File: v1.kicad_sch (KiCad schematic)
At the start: 8 parts, among them J1 Screw_Terminal_01x04, U2 ESP32 DevKitV1 DoIt, U4 AHT20 Humidity Module

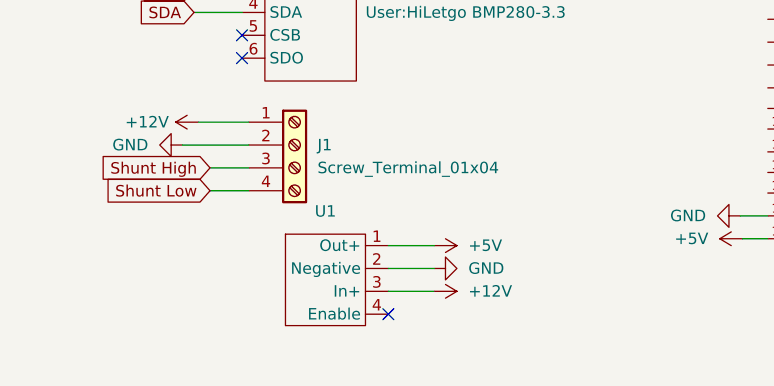
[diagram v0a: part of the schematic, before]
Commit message: Working on alternave voltage converter
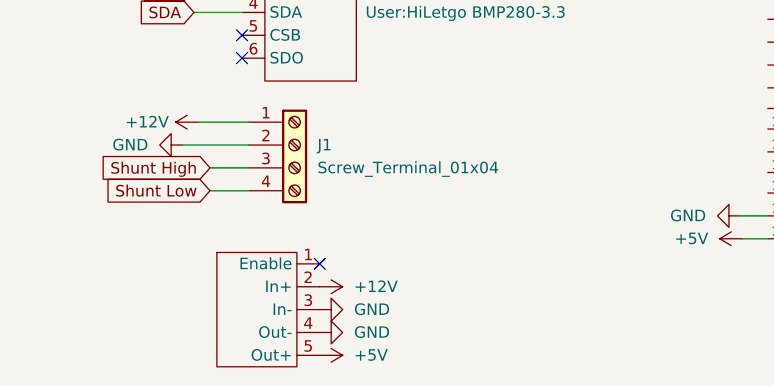
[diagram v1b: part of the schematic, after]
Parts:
- removed U1: ~, User:Drok Vreg, symbol User:Drok_Vreg
- added U5: ~, User:Drok Vreg_5pin, symbol User:Drok_Vreg_5Pin
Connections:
- net +12V: now also U5.2 (In+)
- net +5V: now also U5.5 (Out+)
- net GND: now also U5.3 (In-), U5.4 (Out-)

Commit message: Version 1.2 pcb, 3.3 volt adc, updated step down
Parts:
- R1: value 10000 -> 36000
- R2: value 5000 -> 10000
- renumbered U5 to U1
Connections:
- net +3V3: now also M1.1 (VDD), U1.5 (Out+)
- removed net +5V: M1.1 (VDD), U1.5 (Out+), U2.15 (VIN)
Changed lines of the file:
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@@
 	(wire
 		(pts
-			(xy 96.52 100.076) (xy 99.314 100.076)
+			(xy 37.338 92.202) (xy 41.656 92.202)
 		)
 		(stroke
@@
 	(wire
 		(pts
-			(xy 37.338 92.202) (xy 41.656 92.202)
+			(xy 96.266 97.536) (xy 99.314 97.536)
 		)
 		(stroke
@@
 	(wire
 		(pts
-			(xy 96.266 97.536) (xy 99.314 97.536)
+			(xy 36.068 87.122) (xy 41.656 87.122)
 		)
 		(stroke
@@
 	(wire
 		(pts
-			(xy 36.068 87.122) (xy 41.656 87.122)
+			(xy 25.4 36.068) (xy 29.464 36.068)
 		)
 		(stroke
@@
 	(wire
 		(pts
-			(xy 25.4 36.068) (xy 29.464 36.068)
+			(xy 34.29 89.662) (xy 41.656 89.662)
 		)
 		(stroke
@@
 	(wire
 		(pts
-			(xy 34.29 89.662) (xy 41.656 89.662)
+			(xy 111.76 50.292) (xy 116.332 50.292)
 		)
 		(stroke
@@
 	(wire
 		(pts
-			(xy 111.76 50.292) (xy 116.332 50.292)
+			(xy 43.434 26.416) (xy 43.434 30.988)
 		)
 		(stroke
@@
 	(wire
 		(pts
-			(xy 43.434 26.416) (xy 43.434 30.988)
+			(xy 43.434 52.578) (xy 43.434 56.134)
 		)
 		(stroke
@@
 	(wire
 		(pts
-			(xy 43.434 52.578) (xy 43.434 56.134)
+			(xy 110.49 26.416) (xy 114.3 26.416)
 		)
 		(stroke
@@
 	(wire
 		(pts
-			(xy 110.49 26.416) (xy 114.3 26.416)
+			(xy 124.206 97.79) (xy 130.81 97.79)
 		)
 		(stroke
@@
 	(wire
 		(pts
-			(xy 124.206 97.79) (xy 130.81 97.79)
+			(xy 83.566 26.416) (xy 86.36 26.416)
 		)
 		(stroke
@@
 	(wire
 		(pts
-			(xy 83.566 26.416) (xy 86.36 26.416)
+			(xy 56.134 47.498) (xy 60.96 47.498)
 		)
 		(stroke
@@
 	(wire
 		(pts
-			(xy 56.134 47.498) (xy 60.96 47.498)
+			(xy 99.568 36.068) (xy 99.568 26.416)
 		)
 		(stroke
@@
 	(wire
 		(pts
-			(xy 99.568 36.068) (xy 99.568 26.416)
+			(xy 35.56 67.31) (xy 40.894 67.31)
 		)
 		(stroke
@@
 	(wire
 		(pts
-			(xy 35.56 67.31) (xy 40.894 67.31)
+			(xy 37.338 94.742) (xy 41.656 94.742)
 		)
 		(stroke
@@
 	(wire
 		(pts
-			(xy 37.338 94.742) (xy 41.656 94.742)
+			(xy 56.134 36.068) (xy 99.568 36.068)
 		)
 		(stroke
@@
 	(wire
 		(pts
-			(xy 56.134 36.068) (xy 99.568 36.068)
+			(xy 24.638 43.688) (xy 29.464 43.688)
 		)
 		(stroke
@@
 	(wire
 		(pts
-			(xy 24.638 43.688) (xy 29.464 43.688)
+			(xy 35.56 74.93) (xy 40.894 74.93)
 		)
 		(stroke
@@
 		)
 	)
-	(wire
-		(pts
-			(xy 35.56 74.93) (xy 40.894 74.93)
-		)
-		(stroke
-			(width 0)
-			(type default)
-		)
-	)
 	(global_label "SCL"
 		(shape input)
@@
 	)
 	(symbol
+		(lib_name "GND_3")
 		(lib_id "power:GND")
 		(at 43.434 56.134 0)
@@
 			)
 		)
-		(property "Value" "+5V"
-			(at 43.434 22.098 0)
+		(property "Value" "+3V3"
+			(at 43.434 21.59 0)
 			(effects
 				(font
@@
 	)
 	(symbol
+		(lib_name "GND_4")
 		(lib_id "power:GND")
 		(at 49.53 107.95 90)
@@
 	)
 	(symbol
+		(lib_name "+3V3_2")
 		(lib_id "power:+3V3")
 		(at 116.078 45.212 270)
@@
 	)
 	(symbol
+		(lib_name "GND_1")
 		(lib_id "power:GND")
 		(at 116.332 47.752 90)
@@
 	)
 	(symbol
+		(lib_name "+5V_2")
 		(lib_id "power:+5V")
 		(at 49.53 113.03 270)
@@
 			)
 		)
-		(property "Value" "+5V"
-			(at 53.34 113.03 90)
+		(property "Value" "+3V3"
+			(at 53.34 113.0299 90)
 			(effects
 				(font
@@
 	)
 	(symbol
+		(lib_name "GND_2")
 		(lib_id "power:GND")
 		(at 114.3 26.416 90)
@@
 	)
 	(symbol
+		(lib_name "+12V_2")
 		(lib_id "power:+12V")
 		(at 83.566 26.416 90)
@@
 	)
 	(symbol
-		(lib_id "power:+5V")
-		(at 96.52 100.076 90)
-		(unit 1)
-		(exclude_from_sim no)
-		(in_bom yes)
-		(on_board yes)
-		(dnp no)
-		(property "Reference" "#PWR05"
-			(at 100.33 100.076 0)
-			(effects
-				(font
-					(size 1.27 1.27)
-				)
-				(hide yes)
-			)
-		)
-		(property "Value" "+5V"
-			(at 92.71 100.076 90)
-			(effects
-				(font
-					(size 1.27 1.27)
-				)
-				(justify left)
-			)
-		)
-		(property "Footprint" ""
-			(at 96.52 100.076 0)
-			(effects
-				(font
-					(size 1.27 1.27)
-				)
-				(hide yes)
-			)
-		)
-		(property "Datasheet" ""
-			(at 96.52 100.076 0)
-			(effects
-				(font
-					(size 1.27 1.27)
-				)
-				(hide yes)
-			)
-		)
-		(property "Description" ""
-			(at 96.52 100.076 0)
-			(effects
-				(font
-					(size 1.27 1.27)
-				)
-			)
-		)
-		(pin "1"
-		)
-		(instances
-			(project "BatteryMeter"
-				(path "/70fd842f-e57e-498f-b935-1791177e9c4c"
-					(reference "#PWR05")
-					(unit 1)
-				)
-			)
-		)
-	)
-	(symbol
 		(lib_id "User:ESP32_DevkitV1_DoIt")
 		(at 111.76 63.5 0)
@@
 		(on_board yes)
 		(dnp no)
-		(fields_autoplaced yes)
-		(property "Reference" "U5"
-			(at 42.545 96.52 0)
-			(effects
-				(font
-					(size 1.27 1.27)
-				)
-				(hide yes)
+		(property "Reference" "U1"
+			(at 35.306 102.108 0)
+			(effects
+				(font
+					(size 1.27 1.27)
+				)
 			)
 		)
@@
 		)
 		(property "Footprint" "User:Drok Vreg_5pin"
-			(at 46.99 101.6 0)
-			(effects
-				(font
-					(size 1.27 1.27)
-				)
-				(hide yes)
+			(at 28.194 104.902 0)
+			(effects
+				(font
+					(size 1.27 1.27)
+				)
 			)
 		)
@@
 			(project ""
 				(path "/70fd842f-e57e-498f-b935-1791177e9c4c"
-					(reference "U5")
-					(unit 1)
-				)
-			)
-		)
-	)
-	(symbol
+					(reference "U1")
+					(unit 1)
+				)
+			)
+		)
+	)
+	(symbol
+		(lib_name "+3V3_1")
 		(lib_id "power:+3V3")
 		(at 130.81 100.33 270)
@@
 			)
 		)
-		(property "Value" "5000"
+		(property "Value" "10000"
 			(at 106.68 22.86 90)
 			(effects
@@
 	)
 	(symbol
+		(lib_name "+12V_1")
 		(lib_id "power:+12V")
 		(at 36.068 87.122 90)
@@
 		(fields_autoplaced yes)
 		(property "Reference" "M1"
-			(at 45.6281 31.75 0)
+			(at 45.5773 29.21 0)
 			(effects
 				(font
@@
 		)
 		(property "Value" "~"
-			(at 43.434 41.148 0)
-			(effects
-				(font
-					(size 1.27 1.27)
-				)
+			(at 45.5773 31.75 0)
+			(effects
+				(font
+					(size 1.27 1.27)
+				)
+				(justify left)
 			)
 		)
@@
 					(size 1.27 1.27)
 				)
-				(hide yes)
 			)
 		)
@@
 	)
 	(symbol
+		(lib_name "GND_9")
 		(lib_id "power:GND")
 		(at 49.53 110.49 90)
@@
 	)
 	(symbol
+		(lib_name "GND_8")
 		(lib_id "power:GND")
 		(at 34.29 89.662 270)
@@
 	)
 	(symbol
+		(lib_name "GND_7")
 		(lib_id "power:GND")
 		(at 35.56 69.85 270)
@@
 			)
 		)
-		(property "Value" "10000"
+		(property "Value" "36000"
 			(at 90.17 22.86 90)
 			(effects
@@
 	)
 	(symbol
+		(lib_name "GND_6")
 		(lib_id "power:GND")
 		(at 96.266 97.536 270)
@@
 	)
 	(symbol
+		(lib_name "GND_5")
 		(lib_id "power:GND")
 		(at 24.638 43.688 270)
